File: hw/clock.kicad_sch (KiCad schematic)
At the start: 17 parts, among them Y1201 40MHz, Y1202 Si5351C-B-GM

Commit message: Checkpoint before replicating OSD and then CPLD layout from 0 to 1
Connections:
- net osd1Clk: now also Y1202.8 (CLK3); no longer Y1202.12 (CLK1)
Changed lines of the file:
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@@
+	)
+	(no_connect
+		(at 132.08 82.55)
 	)
 	(no_connect
@@
 	)
 	(no_connect
-		(at 132.08 92.71)
-	)
-	(no_connect
 		(at 101.6 77.47)
 	)
@@
 	(wire
 		(pts
-			(xy 132.08 82.55) (xy 133.35 82.55)
+			(xy 132.08 92.71) (xy 133.35 92.71)
 		)
 		(stroke
@@
 	(hierarchical_label "osd1Clk"
 		(shape output)
-		(at 133.35 82.55 0)
-		(effects
-			(font
+		(at 133.35 92.71 0)
+		(effects
+			(font

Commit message: PCB and schematic both pass DRC and all nets routed. Now for some desk checking...
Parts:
- added R1201: 22, Resistor_SMD:R_0402_1005Metric, symbol Device:R_Small_US
- renumbered R1201 to R1202, R1202 to R1203, R1203 to R1204, R1204 to R1205, R1205 to R1206, R1206 to R1207, R1207 to R1208, R1208 to R1209
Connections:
- net tcxo: now also R1201.2; no longer Y1201.3 (OUTPUT)
- net miscClk: no longer names the net of Y1202.19 (CLK4)
- new net: R1201.1, Y1201.3 (OUTPUT)
- no-connect marks 7 -> 8
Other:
- moved on the sheet: C1206, Y1201

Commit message: 3D rendering now. All DRCs pass on schematic and PCB. BOM scrubbed to coallesce parts. Still no part numbers for most.
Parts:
- C1207: working-voltage 50V -> 25V
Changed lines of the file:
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@@
 			)
 		)
-		(property "working-voltage" "50V"
+		(property "working-voltage" "25V"
 			(at 146.05 118.11 0)
 			(effects

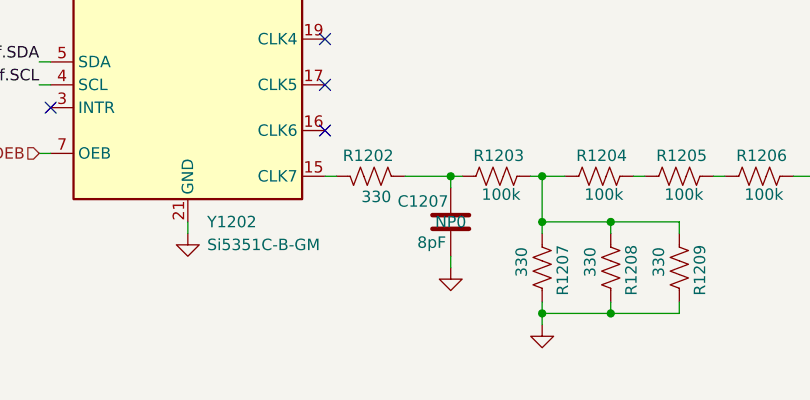
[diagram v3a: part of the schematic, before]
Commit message: Not proud of the rats nest of controls for attenuator and filter, but now I have four filters (not five), all DRC pass, 3D renders properly, and I may tidy it up a bit later.
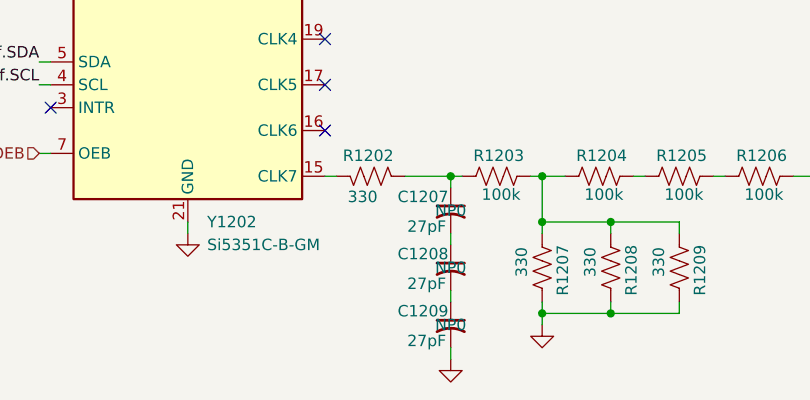
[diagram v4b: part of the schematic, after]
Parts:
- removed C1207: 8pF, Capacitor_SMD:C_0603_1608Metric, symbol Device:C
- added C1207, C1208, C1209: 27pF, Capacitor_SMD:C_0402_1005Metric, symbol Device:C_Small_US
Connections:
- net GND: now also C1209.2
- net at R1202.2, R1203.1: now also C1207.1
- new net: C1207.2, C1208.1
- new net: C1208.2, C1209.1

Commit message: Set up for DVT2 PCBA build at JLCPCB
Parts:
- C1201, C1202, C1203, C1204, C1205, C1206: MPN C0805F104K1RACAUTO -> (none)
- C1207, C1208, C1209: JLCPCBpn C107045 -> (none)
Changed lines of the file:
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@@
 			)
 		)
-		(property "JLCPCBpn" "C107045"
+		(property "JLCPCBpn" ""
 			(at 146.05 123.19 0)
 			(effects
@@
 			)
 		)
-		(property "MPN" "C0805F104K1RACAUTO"
+		(property "MPN" ""
 			(at -50.8 -30.48 0)
 			(effects
@@
 			)
 		)
-		(property "MPN" "C0805F104K1RACAUTO"
+		(property "MPN" ""
 			(at 317.5 -36.83 0)
 			(effects
@@
 			)
 		)
-		(property "JLCPCBpn" "C107045"
+		(property "JLCPCBpn" ""
 			(at 146.05 116.84 0)
 			(effects
@@
 			)
 		)
-		(property "MPN" "C0805F104K1RACAUTO"
+		(property "MPN" ""
 			(at 24.13 -43.18 0)
 			(effects
@@
 			)
 		)
-		(property "JLCPCBpn" "C107045"
+		(property "JLCPCBpn" ""
 			(at 146.05 129.54 0)
 			(effects
@@
 			)
 		)
-		(property "MPN" "C0805F104K1RACAUTO"
+		(property "MPN" ""
 			(at 279.4 -29.21 0)
 			(effects
@@
 			)
 		)
-		(property "MPN" "C0805F104K1RACAUTO"
+		(property "MPN" ""
 			(at -88.9 -35.56 0)
 			(effects
@@
 			)
 		)
-		(property "MPN" "C0805F104K1RACAUTO"
+		(property "MPN" ""
 			(at -96.52 -41.91 0)
 			(effects

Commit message: DVT2 try #2. This is the one from which I ordered PCBs (bare only) from JLCPCB
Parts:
- renumbered Y1202 to U1201
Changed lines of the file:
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@@
 		(dnp no)
 		(fields_autoplaced yes)
-		(property "Reference" "Y1202"
+		(property "Reference" "U1201"
 			(at 118.9833 118.11 0)
 			(effects
@@
 				)
 				(hide yes)
+			)
+		)
+		(property "cap-type" ""
+			(at 116.84 95.25 0)
+			(effects
+				(font
+					(size 1.27 1.27)
+				)
+			)
+		)
+		(property "r-power" ""
+			(at 116.84 95.25 0)
+			(effects
+				(font
+					(size 1.27 1.27)
+				)
+			)
+		)
+		(property "label" ""
+			(at 116.84 95.25 0)
+			(effects
+				(font
+					(size 1.27 1.27)
+				)
 			)
 		)
@@
 			(project "NexRx"
 				(path "/8ae46c04-d01a-4756-8774-512b694bfaff/54a1b66b-2e18-4097-9838-d6ffa2faf921"
-					(reference "Y1202")
+					(reference "U1201")
 					(unit 1)
 				)

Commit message: Switch to parts I can source from Mouser
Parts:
- C1201, C1202, C1203, C1204, C1205, C1206: MFG (none) -> muRata; MPN (none) -> GCM155R71H104KE02D; Mouser Part Number (none) -> 81-GCM155R71H104KE2D
- C1207, C1208, C1209: MFG (none) -> Kyocera; MPN (none) -> 04023A270JAT2A; Mouser Part Number (none) -> 581-04023A270JAT2A
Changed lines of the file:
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@@
 			)
 		)
+		(property "MFG" "Kyocera"
+			(at 146.05 123.19 0)
+			(effects
+				(font
+					(size 1.27 1.27)
+				)
+				(hide yes)
+			)
+		)
+		(property "MPN" "04023A270JAT2A"
+			(at 146.05 123.19 0)
+			(effects
+				(font
+					(size 1.27 1.27)
+				)
+				(hide yes)
+			)
+		)
+		(property "Mouser Part Number" "581-04023A270JAT2A"
+			(at 146.05 123.19 0)
+			(effects
+				(font
+					(size 1.27 1.27)
+				)
+				(hide yes)
+			)
+		)
 		(pin "2"
 		)
@@
 			)
 		)
-		(property "MPN" ""
+		(property "MPN" "GCM155R71H104KE02D"
 			(at -50.8 -30.48 0)
 			(effects
@@
 			)
 		)
+		(property "MFG" "muRata"
+			(at 130.81 66.04 0)
+			(effects
+				(font
+					(size 1.27 1.27)
+				)
+				(hide yes)
+			)
+		)
+		(property "Mouser Part Number" "81-GCM155R71H104KE2D"
+			(at 130.81 66.04 0)
+			(effects
+				(font
+					(size 1.27 1.27)
+				)
+				(hide yes)
+			)
+		)
 		(pin "2"
 		)
@@
 			)
 		)
-		(property "MPN" ""
+		(property "MPN" "GCM155R71H104KE02D"
 			(at 317.5 -36.83 0)
 			(effects
@@
 			)
 		)
+		(property "MFG" "muRata"
+			(at 135.89 59.69 0)
+			(effects
+				(font
+					(size 1.27 1.27)
+				)
+				(hide yes)
+			)
+		)
+		(property "Mouser Part Number" "81-GCM155R71H104KE2D"
+			(at 135.89 59.69 0)
+			(effects
+				(font
+					(size 1.27 1.27)
+				)
+				(hide yes)
+			)
+		)
 		(pin "2"
 		)
@@
 			)
 		)
+		(property "MFG" "Kyocera"
+			(at 146.05 116.84 0)
+			(effects
+				(font
+					(size 1.27 1.27)
+				)
+				(hide yes)
+			)
+		)
+		(property "MPN" "04023A270JAT2A"
+			(at 146.05 116.84 0)
+			(effects
+				(font
+					(size 1.27 1.27)
+				)
+				(hide yes)
+			)
+		)
+		(property "Mouser Part Number" "581-04023A270JAT2A"
+			(at 146.05 116.84 0)
+			(effects
+				(font
+					(size 1.27 1.27)
+				)
+				(hide yes)
+			)
+		)
 		(pin "2"
 		)
@@
 			)
 		)
-		(property "MPN" ""
+		(property "MPN" "GCM155R71H104KE02D"
 			(at 24.13 -43.18 0)
 			(effects
@@
 			)
 		)
+		(property "MFG" "muRata"
+			(at 60.96 99.06 0)
+			(effects
+				(font
+					(size 1.27 1.27)
+				)
+				(hide yes)
+			)
+		)
+		(property "Mouser Part Number" "81-GCM155R71H104KE2D"
+			(at 60.96 99.06 0)
+			(effects
+				(font
+					(size 1.27 1.27)
+				)
+				(hide yes)
+			)
+		)
 		(pin "2"
 		)
@@
 			)
 		)
+		(property "MFG" "Kyocera"
+			(at 146.05 129.54 0)
+			(effects
+				(font
+					(size 1.27 1.27)
+				)
+				(hide yes)
+			)
+		)
+		(property "MPN" "04023A270JAT2A"
+			(at 146.05 129.54 0)
+			(effects
+				(font
+					(size 1.27 1.27)
+				)
+				(hide yes)
+			)
+		)
+		(property "Mouser Part Number" "581-04023A270JAT2A"
+			(at 146.05 129.54 0)
+			(effects
+				(font
+					(size 1.27 1.27)
+				)
+				(hide yes)
+			)
+		)
 		(pin "2"
 		)
@@
 			)
 		)
-		(property "MPN" ""
+		(property "MPN" "GCM155R71H104KE02D"
 			(at 279.4 -29.21 0)
 			(effects
@@
 			)
 		)
+		(property "MFG" "muRata"
+			(at 97.79 67.31 0)
+			(effects
+				(font
+					(size 1.27 1.27)
+				)
+				(hide yes)
+			)
+		)
+		(property "Mouser Part Number" "81-GCM155R71H104KE2D"
+			(at 97.79 67.31 0)
+			(effects
+				(font
+					(size 1.27 1.27)
+				)
+				(hide yes)
+			)
+		)
 		(pin "2"
 		)
@@
 			)
 		)
-		(property "MPN" ""
+		(property "MPN" "GCM155R71H104KE02D"
 			(at -88.9 -35.56 0)
 			(effects
@@
 			)
 		)
+		(property "MFG" "muRata"
+			(at 92.71 60.96 0)
+			(effects
+				(font
+					(size 1.27 1.27)
+				)
+				(hide yes)
+			)
+		)
+		(property "Mouser Part Number" "81-GCM155R71H104KE2D"
+			(at 92.71 60.96 0)
+			(effects
+				(font
+					(size 1.27 1.27)
+				)
+				(hide yes)
+			)
+		)
 		(pin "2"
 		)
@@
 			)
 		)
-		(property "MPN" ""
+		(property "MPN" "GCM155R71H104KE02D"
 			(at -96.52 -41.91 0)
 			(effects
@@
 			(at 85.09 54.61 0)
 			(effects
+				(font
+					(size 1.27 1.27)
+				)
+				(hide yes)
+			)
+		)
+		(property "MFG" "muRata"
+			(at 85.09 54.61 0)
+			(effects
+				(font
+					(size 1.27 1.27)
+				)
+				(hide yes)
+			)
+		)
+		(property "Mouser Part Number" "81-GCM155R71H104KE2D"
+			(at 85.09 54.61 0)
+			(effects

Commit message: Updates for actual DVT2 BOM order part numbers and fixes
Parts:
- R1201: MFG (none) -> Wurth Electronik; MPN (none) -> 560112110216; Mouser Part Number (none) -> 710-560112110216
- R1202, R1207, R1208, R1209: MFG (none) -> YAGEO; MPN (none) -> RC0402JR-7D330RL; Mouser Part Number (none) -> 603-RC0402JR-7D330RL
- R1203, R1204, R1205, R1206: MFG (none) -> YAGEO; MPN (none) -> RP0402BRD07100KL; Mouser Part Number (none) -> 603-RP0402BRD07100KL
- U1201: MFG (none) -> SKYWORKS; MPN (none) -> SI5351C-B-GM; Mouser Part Number (none) -> 634-SI5351C-B-GM
- Y1201: MFG (none) -> ECS; Mouser Part Number (none) -> 520-TXO-2016-33-400T
